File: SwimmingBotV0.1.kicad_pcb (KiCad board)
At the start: 2 copper layers, 74.7 x 44 mm, 130 parts, among them P10 ANT, P11 DEBUG, P2 ANALOG, P3 CHRG, P4 BATT, P6 FIN1, P7 FIN2, P8 MOT1, P9 MOT2, Q1 Q_NMOS_DGS, Q10 PMV45EN2, Q11 PMV45EN2, Q12 PMV45EN2, Q13 PMV45EN2, Q14 PMV45EN2, Q15 PMV45EN2, Q2 Q_NMOS_DGS, Q3 Q_NMOS_DGS, Q4 PMV45EN2, Q5 PMV45EN2, Q6 PMV45EN2, Q7 PMV45EN2, Q8 PMV45EN2, Q9 PMV45EN2, U1 LT3470A, U10 TPS6216X, U11 SST26VF064B, U12 STM32F446-100, U13 LTC1163, U2 MCP73834, U3 A4960, U4 A4960, U5 HUM-900-PRO, U6 MPU-9250, U8 MAX6034_25, U9 TPS6216X, X1 CRYSTAL_SMD, Y1 Crystal

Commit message: commit before I go home
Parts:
- moved C60 21.5 mm to (131.6, 78.4), turned to 270 degrees
- moved C39 20.5 mm to (135.5, 81.4)
- moved C41 18.4 mm to (132.7, 81.4)
- moved C63 9.98 mm to (126.7, 93.2)
- moved C51 5.47 mm to (124.4, 96.3)
- moved R12 4.62 mm to (124.0, 94.5)
- moved C49 3.78 mm to (122.3, 96.5)
- moved R20 3.41 mm to (116.0, 94.0)
- moved R13 3.24 mm to (122.4, 95.3)
- moved R17 2.63 mm to (117.2, 95.5)
- moved R15 2.25 mm to (119.7, 96.3)
- moved C36 1.90 mm to (121.3, 94.0)
- moved C8 1.89 mm to (118.1, 92.7)
- moved C38 1.53 mm to (136.2, 79.3)
- moved C48 0.98 mm to (119.7, 95.0)
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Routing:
- net /Charge/BATT_SEL3: track 8.29 -> 49.9 mm, vias 1 -> 5
- net /Charge/BATT_SEL2: track 4.96 -> 46.2 mm, vias 1 -> 5
- net /Power/AUX_3.3V_GOOD: track 11.4 -> 47.7 mm, vias 1 -> 4
- net /Micro/PD1: track 8.91 -> 41.6 mm, vias 1 -> 4
- net /Micro/PD0: track 15.1 -> 47.5 mm, vias 1 -> 4
- net /Motors/FIN2: track 0.00 -> 21.2 mm, vias 0 -> 1
- net /Motors/FIN1: track 0.00 -> 18.6 mm, vias 0 -> 3
- net /Power/AUX_3.3V_EN: track 14.6 -> 28.4 mm, vias 1 -> 2
- net /Micro/HS_X2: track 0.00 -> 8.77 mm, vias 0 -> 2
- net GND: track 395.5 -> 403.6 mm
- net /Micro/X1: track 0.00 -> 7.34 mm
- net /Micro/HS_X1: track 0.00 -> 5.21 mm
- net /Micro/X2: track 0.00 -> 3.65 mm
- net /Micro/SDIO_CMD: track 0.00 -> 2.33 mm
- net /Micro/RST#: track 0.00 -> 2.21 mm, vias 0 -> 1
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
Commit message: rearranged inputs to all be available for unique interrupts, put unused GPIO on a header for later use
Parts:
- added P5: CONN_01X08, Pin_Headers:Pin_Header_Straight_2x04_Pitch1.27mm, F.Cu at (121.2, 83.2)
- C48, C49, C51, C8, R15: moved to B.Cu
- moved C63 49.2 mm to (129.6, 44.1)
- moved R17 27.3 mm to (140.0, 80.5), turned to 180 degrees
- moved R20 26.8 mm to (140.0, 82.0), turned to 180 degrees
- moved C51 25.7 mm to (127.6, 70.8)
- moved D5 24.1 mm to (142.8, 82.0)
- moved D4 22.2 mm to (142.8, 80.5)
- moved C8 18.7 mm to (118.8, 74.0), turned to 180 degrees
- moved C48 17.6 mm to (130.1, 80.8), turned to 270 degrees
- moved R13 13.5 mm to (133.3, 87.4), turned to 90 degrees
- moved C49 11.8 mm to (127.6, 86.0), turned to 180 degrees
- moved R15 11.7 mm to (125.3, 86.0)
- moved R12 9.98 mm to (131.9, 88.4), turned to 270 degrees
- moved JP1 8.70 mm to (126.8, 88.3)
- moved C36 3.61 mm to (117.8, 94.9)
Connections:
- R17 pad 2: /Micro/PE7 -> /Micro/PE1
- U12 pad 17: /Micro/PC2 -> /Sensors/GYRO_INT
- U12 pad 18: /Sensors/GYRO_INT -> /Micro/PC3
- U12 pad 34: /Micro/PC5 -> /Motors/MOT1_DIAG
- U12 pad 39: /Micro/PE8 -> /Motors/MOT2_CS#
- U12 pad 41: /Motors/MOT2_CS# -> /Micro/PE10
- U12 pad 43: /Motors/MOT2_RESET# -> /Micro/PE12
- U12 pad 56: /Motors/MOT1_DIAG -> /Micro/PD9
- U12 pad 7: /Micro/PC13 -> /Motors/MOT2_RESET#
- U5 pad 13: /Micro/PE1 -> /Micro/PE15
- U5 pad 31: /Micro/PE13 -> /Micro/PE10
- U5 pad 7: /Micro/PB14 -> /Micro/PE12
- U9 pad 3: /Micro/PD0 -> /Micro/PD1
- U9 pad 8: /Micro/PD1 -> /Micro/PD0
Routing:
- net /Micro/PB14: track 37.5 -> 0.00 mm, vias 2 -> 0
- net /Micro/PE12: track 0.00 -> 35.4 mm, vias 0 -> 2
- net /Micro/PE15: track 0.00 -> 17.1 mm, vias 0 -> 1
- net /Micro/PE1: track 17.1 -> 0.00 mm, vias 1 -> 0
- net /Micro/PD0: track 47.5 -> 39.7 mm, vias 4 -> 3
- net /Sensors/GYRO_FSYNC: track 5.41 -> 0.00 mm
- net /Micro/PD1: track 41.6 -> 46.0 mm, vias 4 -> 3

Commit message: autosave
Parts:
- C36, C46, R13: moved to B.Cu
- C51: moved to F.Cu
- moved C46 16.9 mm to (131.8, 81.4), turned to 180 degrees
- moved C36 12.3 mm to (118.8, 82.6), turned to 270 degrees
- moved P9 9.82 mm to (156.6, 69.8), turned to 180 degrees
- moved C51 7.98 mm to (135.0, 73.8), turned to 90 degrees
- moved R17 4.42 mm to (137.3, 84.0)
- moved D4 3.72 mm to (140.0, 83.0)
- moved P5 3.13 mm to (124.0, 81.8), turned to 270 degrees
- moved D5 2.93 mm to (140.0, 81.0)
- moved R20 2.75 mm to (137.3, 82.5)
- moved C6 2.00 mm to (133.6, 73.8), turned to 90 degrees
- moved R13 1.40 mm to (131.9, 87.5)
- moved P2 1.31 mm to (139.8, 74.8), turned to 270 degrees
- moved C8 1.10 mm to (118.9, 72.9)
- moved C35 0.82 mm to (142.1, 88.8)
- moved U6 0.72 mm to (142.3, 86.4)
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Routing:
- net GND: track 403.6 -> 463.4 mm, vias 49 -> 52
- net /Micro/SWCLK: track 0.00 -> 46.6 mm, vias 0 -> 2
- net /Micro/BOOT0: track 0.00 -> 43.7 mm, vias 0 -> 5
- net /Power/CHG_CTL_VCC: track 69.7 -> 111.5 mm, vias 7 -> 11
- net /Micro/SWDIO: track 0.00 -> 40.7 mm, vias 0 -> 2
- net /Sensors/GYRO_INT: track 0.00 -> 28.5 mm, vias 0 -> 4
- net /Sensors/GYRO_FSYNC: track 0.00 -> 28.5 mm, vias 0 -> 4
- net /Micro/PE12: track 35.4 -> 11.0 mm, vias 2 -> 0
- net /Micro/RST#: track 2.21 -> 24.1 mm, vias 1 -> 5
- net /Micro/SCL: track 3.46 -> 24.3 mm, vias 0 -> 2
- net /Motors/MOT2_RESET#: track 0.00 -> 20.8 mm, vias 0 -> 2
- net /Micro/SDA: track 5.09 -> 25.8 mm, vias 1 -> 2
- net /Motors/C2: track 9.62 -> 29.9 mm
- net /Digital/CE#: track 0.00 -> 18.2 mm, vias 0 -> 1
- net /Motors/SDO: track 28.9 -> 47.0 mm, vias 3 -> 4
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
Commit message: end of day, two lines left to connect
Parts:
- C47, C7: moved to B.Cu
- moved P8 32.1 mm to (124.9, 66.1), turned to 90 degrees
- moved C7 28.8 mm to (139.6, 48.0)
- moved C63 12.1 mm to (140.2, 50.0), turned to 180 degrees
- moved C47 4.08 mm to (113.7, 74.1), turned to 270 degrees
- moved R18 2.27 mm to (129.5, 64.2)
- turned C8 to 0 degrees
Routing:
- net /Digital/3.3V: track 69.5 -> 146.8 mm, vias 7 -> 14
- net GND: track 463.4 -> 534.3 mm, vias 52 -> 61
- net /Micro/MOT1_PWM: track 0.67 -> 48.6 mm, vias 0 -> 2
- net /Motors/MOT1_DIAG: track 0.67 -> 45.8 mm, vias 0 -> 2
- net /Motors/MOT1_TACH: track 0.67 -> 42.6 mm, vias 0 -> 2
- net /Motors/MOT2_TACH: track 0.67 -> 42.3 mm, vias 0 -> 4
- net /Micro/MOT2_PWM: track 0.67 -> 39.5 mm, vias 0 -> 4
- net /Motors/MOT1_RESET#: track 0.70 -> 39.5 mm, vias 0 -> 2
- net /Motors/MOT2_DIAG: track 0.67 -> 38.8 mm, vias 0 -> 2
- net /Power/CHG_CTL_VCC: track 111.5 -> 146.1 mm, vias 11 -> 14
- net /Motors/MOT1_CS#: track 0.00 -> 34.5 mm, vias 0 -> 4
- net /Motors/MOT2_CS#: track 0.00 -> 31.3 mm, vias 0 -> 4
- net /Micro/PE12: track 11.0 -> 40.1 mm, vias 0 -> 2
- net /Micro/PE15: track 17.1 -> 45.5 mm, vias 1 -> 2
- net /Motors/MOT2_RESET#: track 20.8 -> 48.2 mm, vias 2 -> 4
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
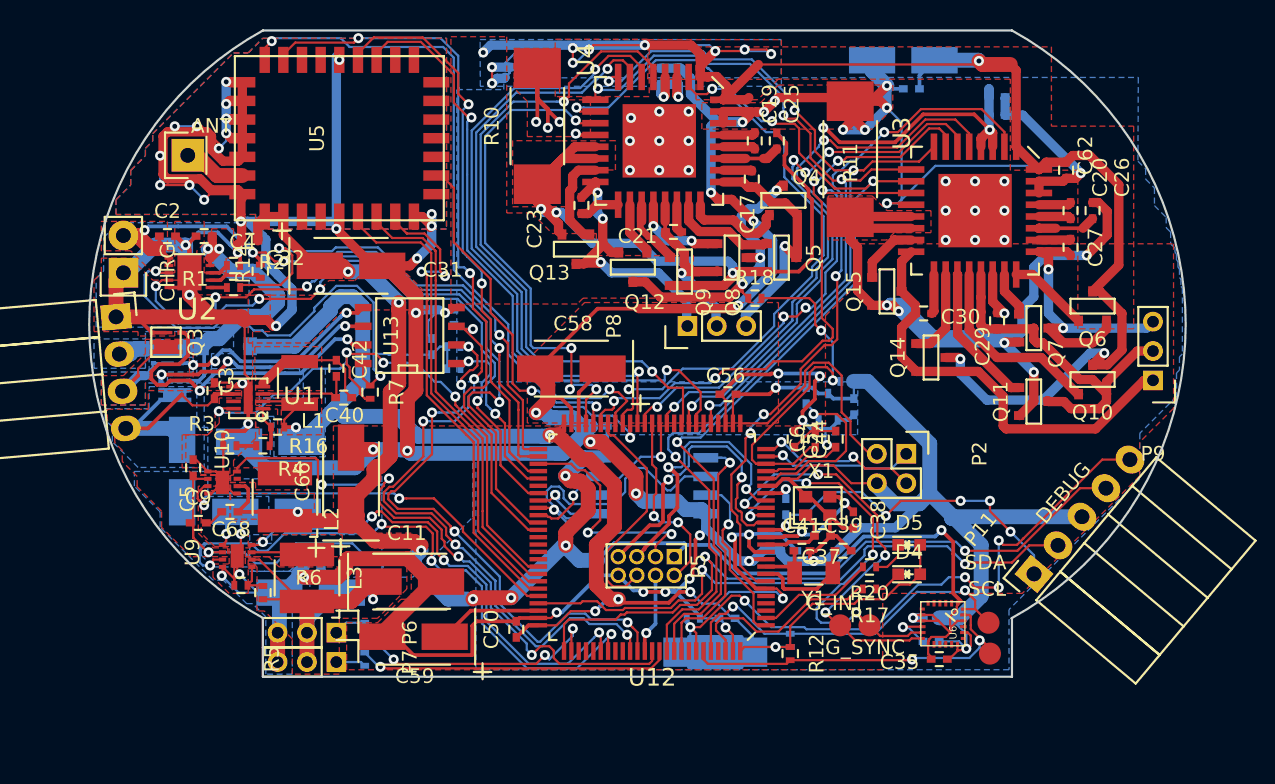
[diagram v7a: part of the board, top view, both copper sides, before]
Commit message: different solder bridge, done with routing, moving silk layer around now
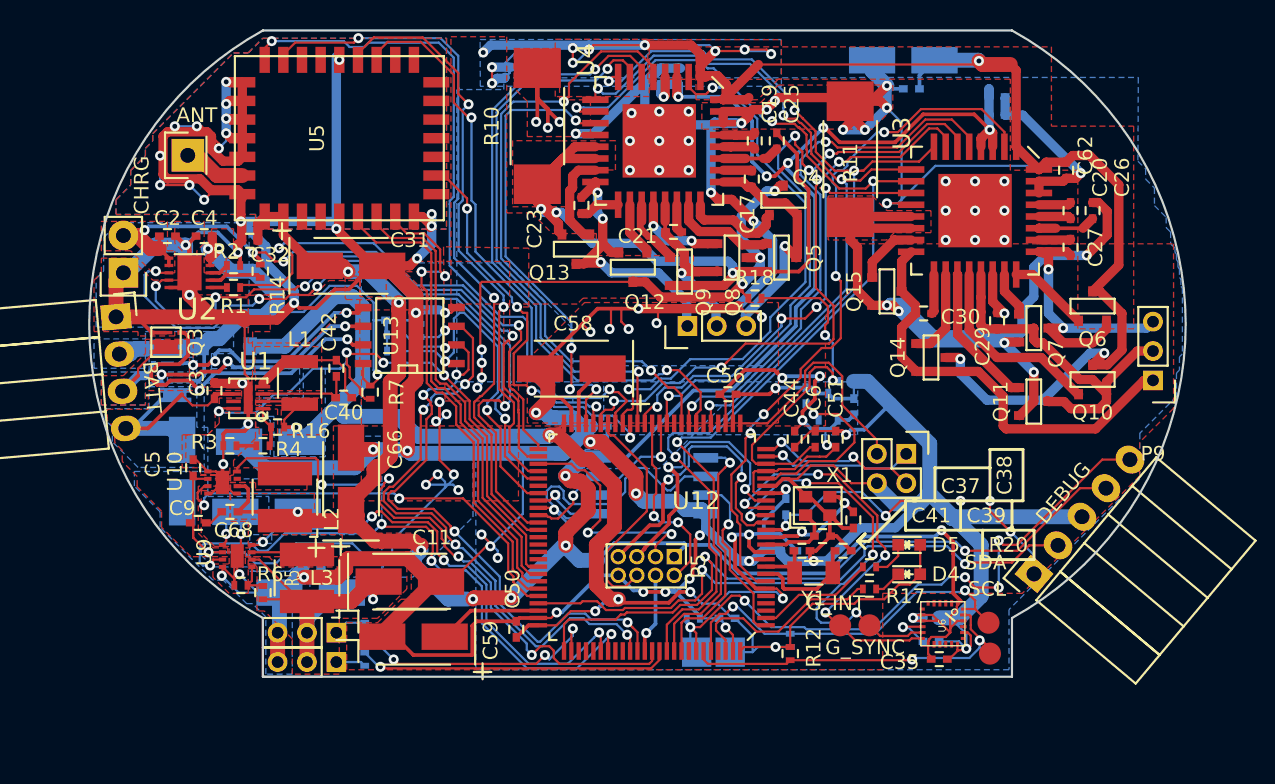
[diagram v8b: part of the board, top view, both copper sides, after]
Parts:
- D4: value LED -> eLED
- JP1: footprint Oddities:NetTie-I_Connected_SMD -> Custom_Footprints:SOLDER-JUMPER
- moved R22 4.27 mm to (104.9, 67.8)
- moved R21 4.18 mm to (104.9, 66.7)
- moved C13 3.16 mm to (104.9, 65.7), turned to 0 degrees
- moved R23 2.47 mm to (106.7, 66.4)
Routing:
- net GND: track 534.3 -> 579.5 mm, vias 61 -> 71
- net /Digital/3.3V: track 146.8 -> 191.6 mm, vias 14 -> 16
- net /Charge/2S: track 194.3 -> 232.0 mm, vias 17 -> 28
- net /Charge/BATT_SEL1: track 14.4 -> 23.6 mm
- net /Power/CHG_CTL_VCC: track 146.1 -> 153.9 mm
- net /Charge/1S: track 61.9 -> 58.1 mm
- net /Charge/BATT_SEL2: track 41.1 -> 44.1 mm
- net /Micro/MOT1_PWM: track 48.6 -> 45.7 mm
- net /Motors/MOT1_DIAG: track 45.8 -> 43.0 mm
- net /Micro/MOT2_PWM: track 39.5 -> 42.1 mm
- net Net-(U4-PadPAD): track 4.00 -> 6.67 mm
- net /Motors/MOT1_CS#: track 34.5 -> 31.9 mm
- net /Motors/MOT1_TACH: track 42.6 -> 40.0 mm
- net /Motors/MOT2_DIAG: track 38.8 -> 37.5 mm
- net /Micro/PE15: track 45.5 -> 46.7 mm
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- added copper zone on B.Cu, net /Digital/3.3V
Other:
- outline, holes or cut-outs redrawn
